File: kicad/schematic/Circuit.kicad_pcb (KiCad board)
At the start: 2 copper layers, 66 parts, among them P1 LED+, P10 1MTR+, P11 1MTR+, P12 1MTR+, P13 1MTR+, P14 1MTR+, P15 1MTR+, P16 1MTR+, P17 1MTR+, P18 1MTR+, P19 1MTR+, P2 LED+, P20 1MTR+, P22 1MTR+, P3 LED+, P4 PWR+, P5 PWR-, P6 1MTR+, P7 1MTR+, P8 1MTR+, P9 1MTR+, Q1 AO3400A, Q2 AO3400A, Q3 AO3400A, Q4 AO3400A, Q5 AO3400A, Q6 AO3400A, Q7 AO3400A, Q8 AO3400A

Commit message: changed board layout. WIP
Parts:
- removed P1, P2, P3: LED+, Connector_Wire:SolderWirePad_1x01_SMD_1x2mm
- removed P10, P11, P12, P13, P14, P15, P16, P17, P18, P19, P20, P22, P6, P7, P8, P9: 1MTR+, Connector_Wire:SolderWirePad_1x01_SMD_1x2mm
- removed P4: PWR+, Connector_Wire:SolderWirePad_1x01_SMD_1x2mm
- removed P5: PWR-, Connector_Wire:SolderWirePad_1x01_SMD_1x2mm
- added BAT+1: ~, ESP_global:blank pad, F.Cu at (162.6, 87.0)
- added BAT-1: ~, ESP_global:blank pad, F.Cu at (162.6, 89.5)
- added C9: C_Polarized, Capacitor_SMD:CP_Elec_8x10.5, F.Cu at (209.6, 94.5)
- added R19: R, Resistor_SMD:R_0805_2012Metric, F.Cu at (205.1, 102.5)
- added RGB-DIN1: ~, ESP_global:blank pad, F.Cu at (205.1, 107.3)
- added RGB-VDD1: ~, ESP_global:blank pad, F.Cu at (207.6, 107.3)
- added RGB-gnd1: ~, ESP_global:blank pad, F.Cu at (210.2, 107.3)
- added m1+1: ~, ESP_global:blank pad, F.Cu at (227.3, 64.1)
- added m1-1: ~, ESP_global:blank pad, F.Cu at (227.3, 61.6)
- added m2+1: ~, ESP_global:blank pad, F.Cu at (227.3, 70.5)
- added m2-1: ~, ESP_global:blank pad, F.Cu at (227.3, 67.9)
- added m3+1: ~, ESP_global:blank pad, F.Cu at (227.3, 76.8)
- added m3-1: ~, ESP_global:blank pad, F.Cu at (227.3, 74.3)
- added m4+1: ~, ESP_global:blank pad, F.Cu at (227.3, 83.2)
- added m4-1: ~, ESP_global:blank pad, F.Cu at (227.3, 80.6)
- added m5+1: ~, ESP_global:blank pad, F.Cu at (227.3, 89.5)
- added m5-1: ~, ESP_global:blank pad, F.Cu at (227.3, 87.0)
- added m6+1: ~, ESP_global:blank pad, F.Cu at (215.9, 107.3)
- added m6-1: ~, ESP_global:blank pad, F.Cu at (213.4, 107.3)
- added m7+1: ~, ESP_global:blank pad, F.Cu at (219.7, 107.3)
- added m7-1: ~, ESP_global:blank pad, F.Cu at (222.2, 107.3)
- added m8+1: ~, ESP_global:blank pad, F.Cu at (226.1, 107.3)
- added m8-1: ~, ESP_global:blank pad, F.Cu at (228.6, 107.3)
- R17: value R 20k -> R
- R18: value R 10k -> R
- moved U2 111.1 mm to (198.1, 97.2), turned to 90 degrees
- moved Q8 105.7 mm to (197.2, 62.9)
- moved C8 105.4 mm to (228.0, 95.2), turned to -90 degrees
- moved R17 98.6 mm to (178.2, 89.5)
- moved D8 97.9 mm to (227.3, 100.9)
- moved R18 97.0 mm to (183.2, 89.5)
- moved C7 96.5 mm to (223.5, 95.2), turned to -90 degrees
- moved D7 89.1 mm to (222.9, 100.9)
- moved C6 88.7 mm to (218.4, 94.9), turned to -90 degrees
- moved Q7 86.5 mm to (197.2, 79.4)
- moved Q4 86.5 mm to (209.9, 83.2)
- moved Q6 85.5 mm to (197.2, 71.1)
- moved R8 85.3 mm to (205.4, 76.2), turned to 0 degrees
- moved R3 85.0 mm to (205.5, 73.7), turned to 0 degrees
- moved Q3 84.9 mm to (209.9, 78.1)
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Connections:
- ESP32_S3_ZERO1 pad 8: unconnected-(ESP32_S3_ZERO1-GP5-Pad8) -> Net-(ESP32_S3_ZERO1-GP5)
- R10 pad 1: Net-(Q4-G) -> Net-(ESP32_S3_ZERO1-GP9)
- R12 pad 1: Net-(Q6-G) -> Net-(ESP32_S3_ZERO1-GP8)
- R14 pad 1: Net-(Q7-G) -> Net-(ESP32_S3_ZERO1-GP7)
- R16 pad 1: Net-(Q8-G) -> Net-(ESP32_S3_ZERO1-GP6)
- R6 pad 1: Net-(Q5-G) -> Net-(ESP32_S3_ZERO1-GP13)
- R7 pad 1: Net-(Q1-G) -> Net-(ESP32_S3_ZERO1-GP12)
- R8 pad 1: Net-(Q2-G) -> Net-(ESP32_S3_ZERO1-GP11)
- R9 pad 1: Net-(Q3-G) -> Net-(ESP32_S3_ZERO1-GP10)
- U1 pad 5: Net-(D1-K) -> Net-(U1-OUT+)
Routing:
- net GND: track 259.1 -> 0.00 mm, vias 21 -> 0
- net Net-(D1-K): track 257.6 -> 0.00 mm, vias 12 -> 0
- net GND1: track 82.8 -> 0.00 mm, vias 2 -> 0
- net Net-(ESP32_S3_ZERO1-GP7): track 67.4 -> 0.00 mm, vias 4 -> 0
- net Net-(ESP32_S3_ZERO1-GP13): track 63.8 -> 0.00 mm, vias 4 -> 0
- net Net-(ESP32_S3_ZERO1-GP8): track 60.9 -> 0.00 mm, vias 4 -> 0
- net Net-(ESP32_S3_ZERO1-GP9): track 53.7 -> 0.00 mm, vias 4 -> 0
- net Net-(ESP32_S3_ZERO1-GP6): track 53.5 -> 0.00 mm, vias 2 -> 0
- net Net-(ESP32_S3_ZERO1-GP12): track 49.8 -> 0.00 mm, vias 4 -> 0
- net Net-(ESP32_S3_ZERO1-GP10): track 47.2 -> 0.00 mm, vias 4 -> 0
- net Net-(ESP32_S3_ZERO1-GP11): track 39.2 -> 0.00 mm, vias 2 -> 0
- net Net-(ESP32_S3_ZERO1-5V): track 34.5 -> 0.00 mm, vias 4 -> 0
- net Net-(ESP32_S3_ZERO1-GP1): track 16.4 -> 0.00 mm, vias 2 -> 0
- net Net-(D6-A): track 12.4 -> 0.00 mm
- net Net-(D8-A): track 12.3 -> 0.00 mm
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
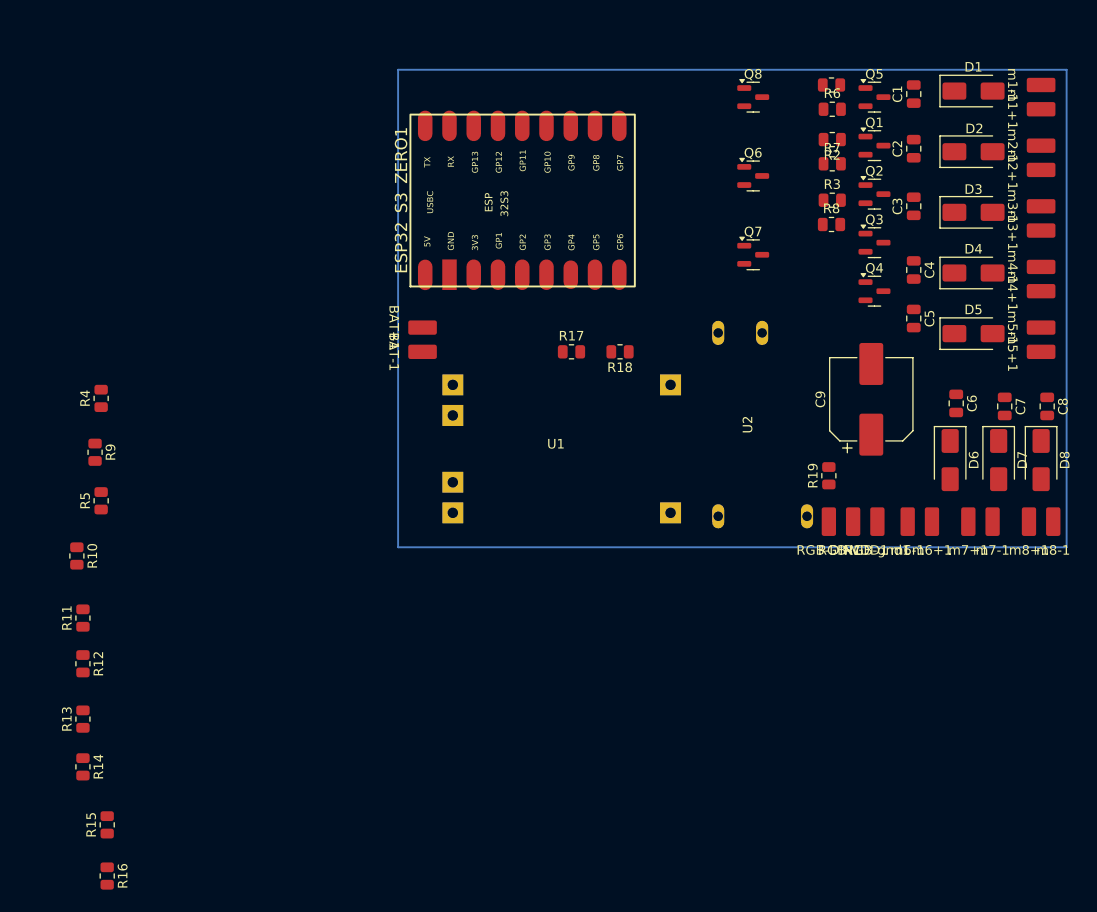
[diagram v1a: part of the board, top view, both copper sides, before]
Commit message: Alle Komponenten auf dem Board - Leiterbahnen verlegt
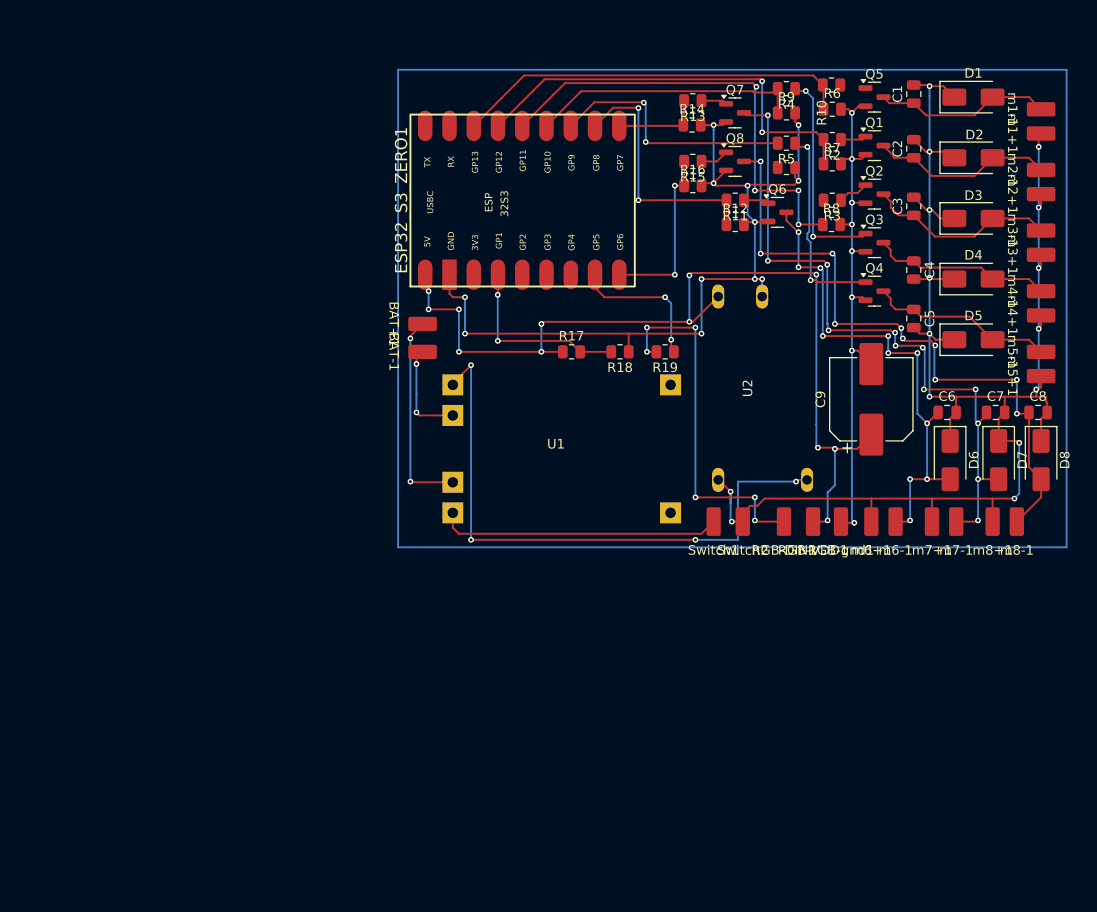
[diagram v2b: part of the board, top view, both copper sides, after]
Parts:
- added Switch1: ~, ESP_global:blank pad, F.Cu at (193.0, 107.3)
- added Switch2: ~, ESP_global:blank pad, F.Cu at (196.1, 107.3)
- moved R16 94.8 mm to (190.9, 72.1), turned to 0 degrees
- moved R15 92.7 mm to (190.9, 69.6), turned to 180 degrees
- moved R14 92.7 mm to (190.8, 65.8), turned to 0 degrees
- moved R13 90.9 mm to (190.9, 63.2), turned to 180 degrees
- moved R10 84.7 mm to (200.7, 70.2), turned to 0 degrees
- moved R12 82.3 mm to (195.3, 76.2), turned to 0 degrees
- moved R11 81.1 mm to (195.3, 73.7), turned to 180 degrees
- moved R5 80.9 mm to (200.7, 67.7), turned to 180 degrees
- moved R9 80.6 mm to (200.7, 64.5), turned to 0 degrees
- moved R4 78.7 mm to (200.7, 62.0), turned to 180 degrees
- moved R19 21.5 mm to (188.0, 89.5), turned to 180 degrees
- moved Q7 15.0 mm to (195.3, 64.5)
- moved Q8 7.00 mm to (195.3, 69.6)
- moved m6+1 6.35 mm to (209.6, 107.3)
- moved RGB-DIN1 4.70 mm to (200.4, 107.3)
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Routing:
- net Net-(D1-K): track 0.00 -> 170.4 mm, vias 0 -> 15
- net GND: track 0.00 -> 150.1 mm, vias 0 -> 20
- net Net-(ESP32_S3_ZERO1-5V): track 0.00 -> 97.0 mm, vias 0 -> 12
- net Net-(D7-A): track 0.00 -> 72.4 mm, vias 0 -> 12
- net Net-(D8-A): track 0.00 -> 68.5 mm, vias 0 -> 10
- net GND1: track 0.00 -> 62.5 mm, vias 0 -> 4
- net Net-(D6-A): track 0.00 -> 53.4 mm, vias 0 -> 11
- net Net-(ESP32_S3_ZERO1-GP11): track 0.00 -> 48.1 mm, vias 0 -> 4
- net Net-(ESP32_S3_ZERO1-GP12): track 0.00 -> 44.4 mm, vias 0 -> 2
- net Net-(ESP32_S3_ZERO1-GP13): track 0.00 -> 41.7 mm
- net Net-(RGB-DIN1-pin): track 0.00 -> 38.1 mm, vias 0 -> 6
- net Net-(Switch1-pin): track 0.00 -> 29.7 mm
- net Net-(ESP32_S3_ZERO1-GP10): track 0.00 -> 28.5 mm
- net Net-(ESP32_S3_ZERO1-GP9): track 0.00 -> 26.8 mm, vias 0 -> 2
- net Net-(ESP32_S3_ZERO1-GP8): track 0.00 -> 26.8 mm, vias 0 -> 2
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
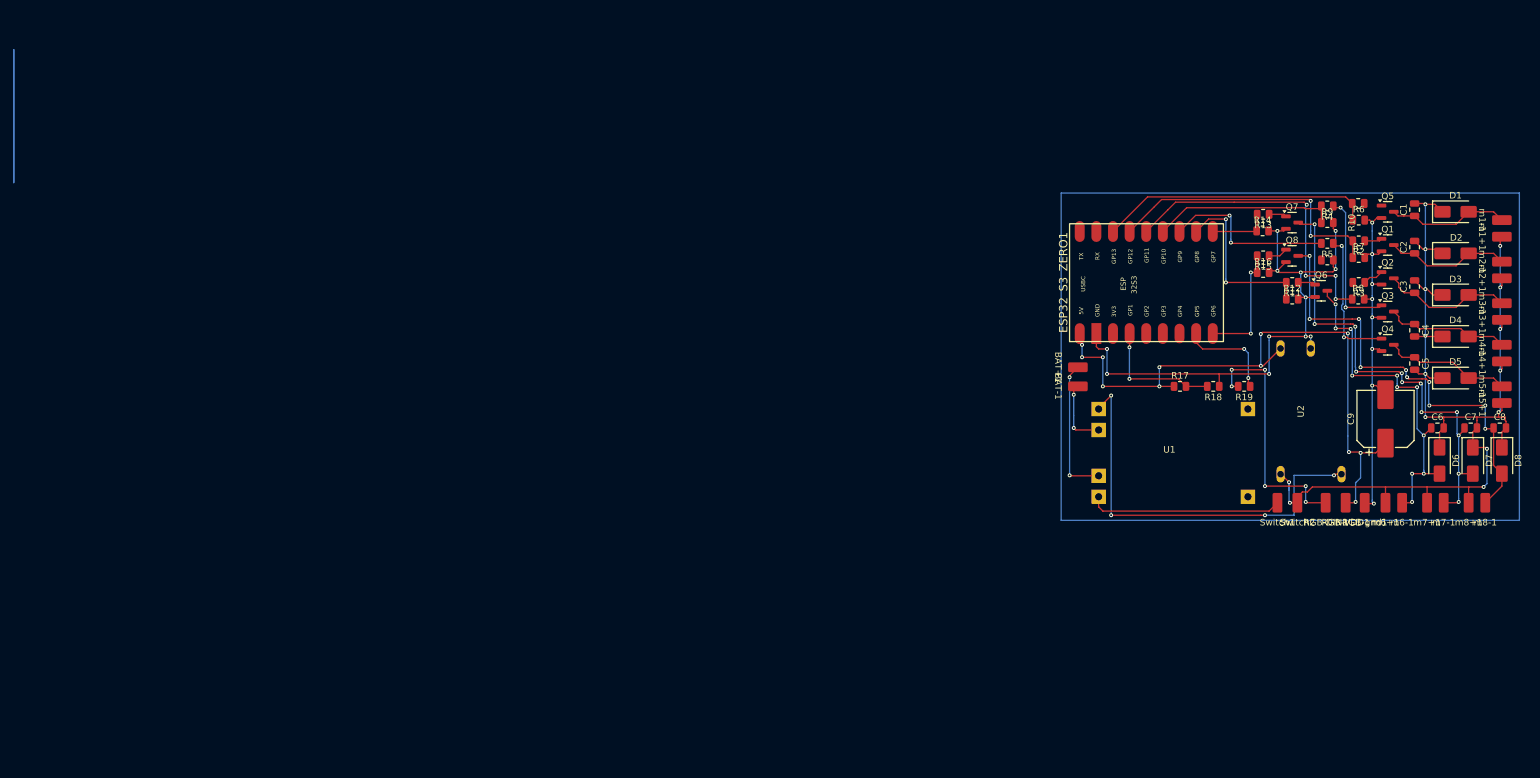
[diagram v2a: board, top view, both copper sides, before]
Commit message: fixed board size beschriftungen verbessert
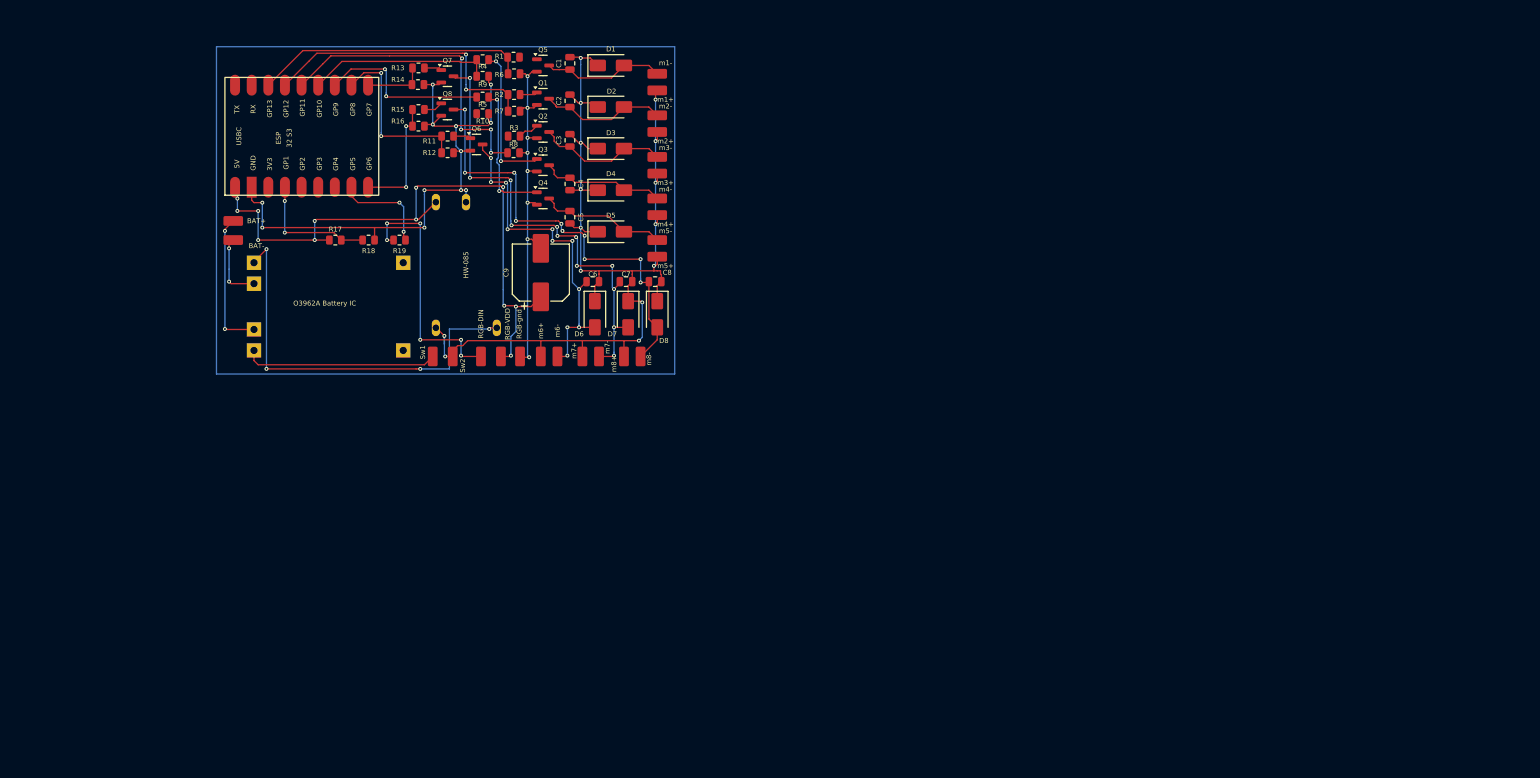
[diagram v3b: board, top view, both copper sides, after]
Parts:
- O3962A Battery IC: renamed from U1
- moved BAT+ 131.0 mm to (33.5, 64.3)
- moved BAT- 131.0 mm to (33.5, 67.2)
- moved C1 131.0 mm to (85.0, 40.2)
- moved C2 131.0 mm to (85.0, 45.9)
- moved C3 131.0 mm to (85.0, 51.9)
- moved C4 131.0 mm to (85.0, 58.6)
- moved C5 131.0 mm to (85.0, 63.7)
- moved C6 131.0 mm to (88.5, 73.5)
- moved C9 131.0 mm to (80.5, 72.2)
- moved D6 131.0 mm to (88.8, 78.5)
- moved D8 131.0 mm to (98.3, 78.5)
- moved HW-085 131.0 mm to (69.1, 71.0)
- moved O3962A Battery IC 131.0 mm to (47.5, 77.3)
- moved R11 131.0 mm to (66.3, 51.3)
- moved R12 131.0 mm to (66.3, 53.8)
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- renumbered BAT+1 to BAT+, BAT-1 to BAT-, U2 to HW-085, RGB-DIN1 to RGB-DIN, RGB-VDD1 to RGB-VDD, RGB-gnd1 to RGB-gnd, Switch1 to Sw1, Switch2 to Sw2, m1+1 to m1+, m1-1 to m1-, m2+1 to m2+, m2-1 to m2-, m3+1 to m3+, m3-1 to m3-, m4+1 to m4+, m4-1 to m4-, m5+1 to m5+, m5-1 to m5-, m6+1 to m6+, m6-1 to m6-, m7+1 to m7+, m7-1 to m7-, m8+1 to m8+, m8-1 to m8-
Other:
- board text added: "R1"
- board text added: "R13"
- board text added: "R14"

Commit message: turned Charging moved esp
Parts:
- moved O3962A Battery IC 2.29 mm to (45.2, 77.3), turned to 180 degrees
- moved ESP32_S3_ZERO1 2.01 mm to (46.0, 51.3)
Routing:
- net GND1: track 62.5 -> 25.1 mm, vias 4 -> 1
- net Net-(BAT-1-pin): track 10.5 -> 36.0 mm, vias 2 -> 1
- net Net-(BAT+1-pin): track 21.5 -> 31.4 mm, vias 2 -> 1
- net Net-(Switch1-pin): track 29.7 -> 20.5 mm, vias 0 -> 1
- net GND: track 150.1 -> 154.7 mm
- net Net-(Q5-G): track 0.00 -> 2.78 mm
- net Net-(ESP32_S3_ZERO1-GP1): track 19.3 -> 17.3 mm
- net Net-(ESP32_S3_ZERO1-GP6): track 18.7 -> 16.6 mm
- net Net-(ESP32_S3_ZERO1-GP7): track 9.32 -> 7.31 mm
- net Net-(ESP32_S3_ZERO1-5V): track 97.0 -> 95.2 mm, vias 12 -> 10
- net Net-(ESP32_S3_ZERO1-GP5): track 15.2 -> 13.8 mm
- net Net-(ESP32_S3_ZERO1-GP12): track 44.4 -> 43.6 mm
- net Net-(ESP32_S3_ZERO1-GP10): track 28.5 -> 27.6 mm
- net Net-(ESP32_S3_ZERO1-GP13): track 41.7 -> 40.9 mm
- net Net-(ESP32_S3_ZERO1-GP11): track 48.1 -> 47.3 mm
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
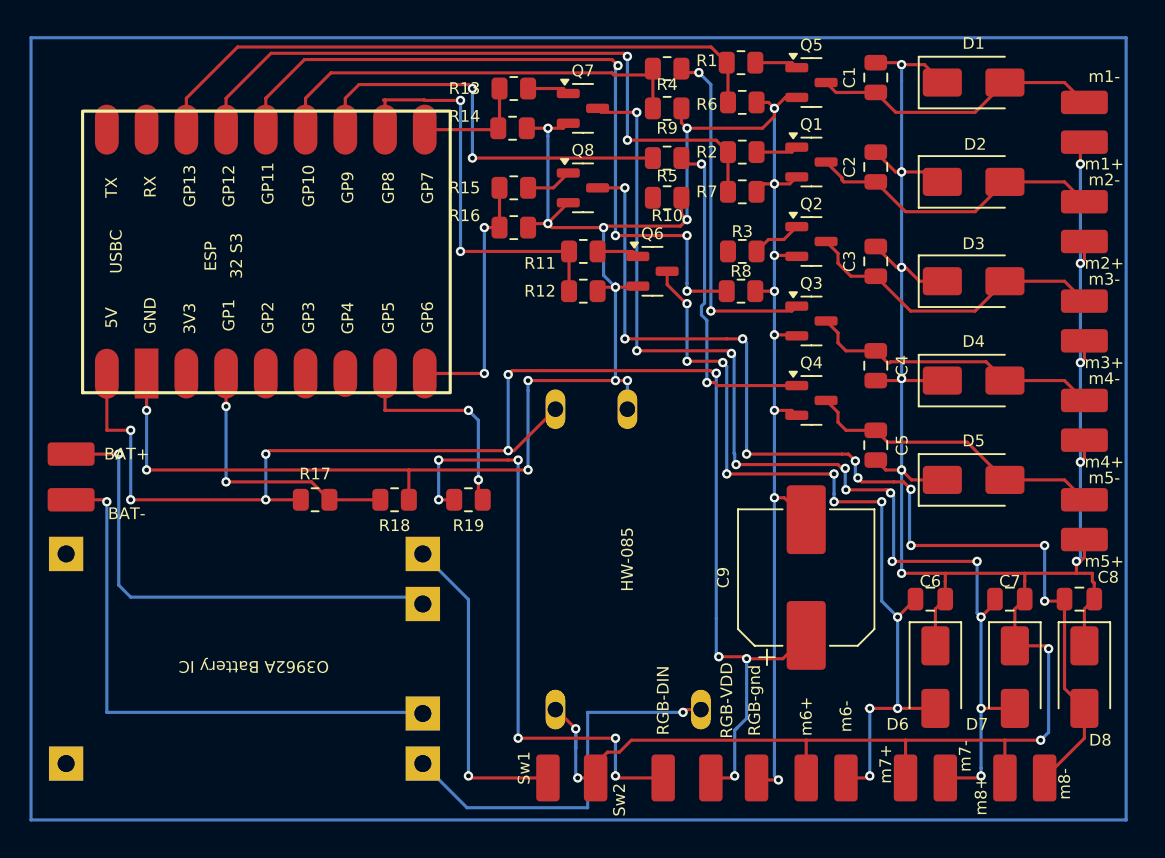
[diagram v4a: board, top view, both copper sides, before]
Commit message: changed pads HW-085
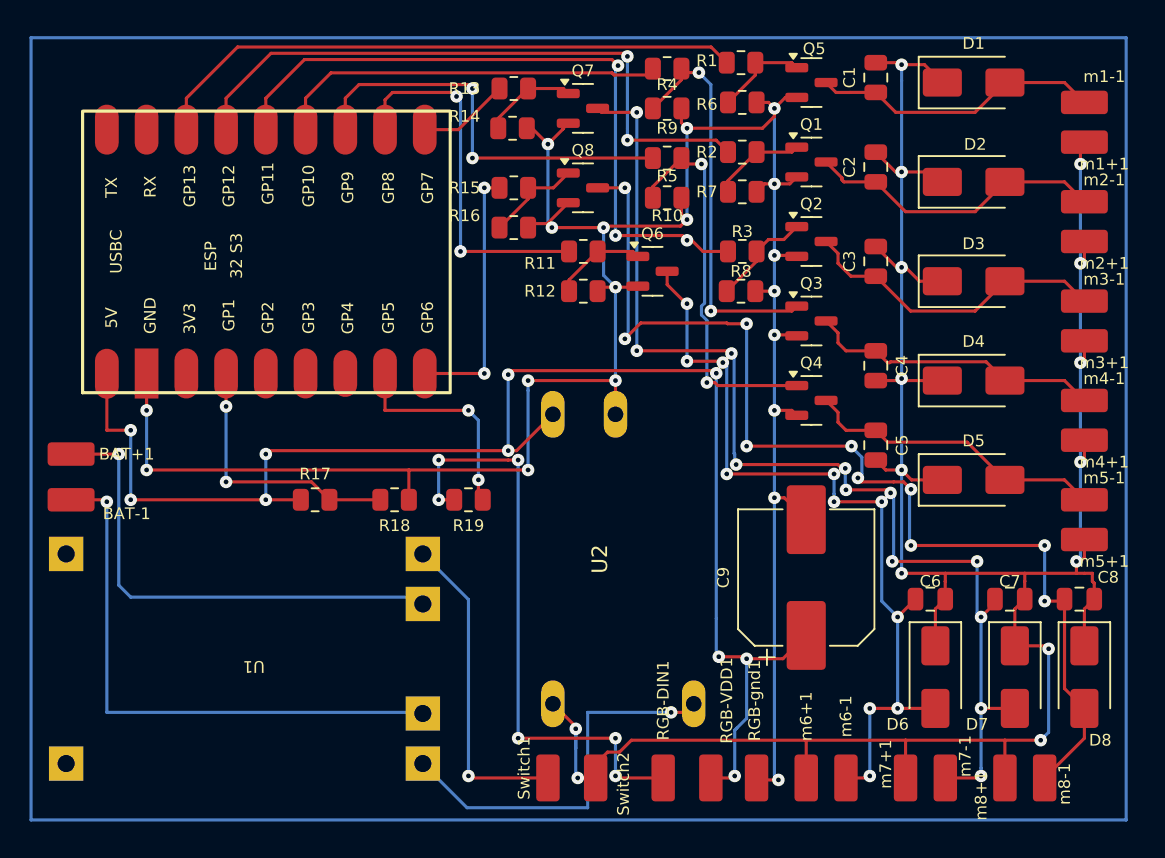
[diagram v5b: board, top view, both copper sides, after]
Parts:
- removed HW-085: ~, ESP_global:HW-085
- added U2: ~, ESP_global:HW-085, F.Cu at (68.8, 71.0)
- U1: renamed from O3962A Battery IC
- renumbered BAT+ to BAT+1, BAT- to BAT-1, RGB-DIN to RGB-DIN1, RGB-VDD to RGB-VDD1, RGB-gnd to RGB-gnd1, Sw1 to Switch1, Sw2 to Switch2, m1+ to m1+1, m1- to m1-1, m2+ to m2+1, m2- to m2-1, m3+ to m3+1, m3- to m3-1, m4+ to m4+1, m4- to m4-1, m5+ to m5+1, m5- to m5-1, m6+ to m6+1, m6- to m6-1, m7+ to m7+1, m7- to m7-1, m8+ to m8+1, m8- to m8-1
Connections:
- R10 pad 1: Net-(ESP32_S3_ZERO1-GP9) -> Net-(Q4-G)
- R12 pad 1: Net-(ESP32_S3_ZERO1-GP8) -> Net-(Q6-G)
- R14 pad 1: Net-(ESP32_S3_ZERO1-GP7) -> Net-(Q7-G)
- R16 pad 1: Net-(ESP32_S3_ZERO1-GP6) -> Net-(Q8-G)
- R6 pad 1: Net-(ESP32_S3_ZERO1-GP13) -> Net-(Q5-G)
- R7 pad 1: Net-(ESP32_S3_ZERO1-GP12) -> Net-(Q1-G)
- R8 pad 1: Net-(ESP32_S3_ZERO1-GP11) -> Net-(Q2-G)
- R9 pad 1: Net-(ESP32_S3_ZERO1-GP10) -> Net-(Q3-G)
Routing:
- net Net-(Q2-G): track 3.23 -> 6.56 mm
- net Net-(Q7-G): track 2.70 -> 6.03 mm
- net Net-(Q8-G): track 2.96 -> 6.26 mm
- net Net-(Q1-G): track 2.70 -> 6.00 mm
- net Net-(Q6-G): track 2.70 -> 6.00 mm
- net Net-(Q4-G): track 21.5 -> 24.8 mm
- net Net-(Q3-G): track 22.4 -> 25.7 mm
- net Net-(Q5-G): track 2.78 -> 6.05 mm
- net Net-(ESP32_S3_ZERO1-GP11): track 47.3 -> 44.2 mm, vias 4 -> 3
- net Net-(ESP32_S3_ZERO1-GP13): track 40.9 -> 38.3 mm
- net Net-(ESP32_S3_ZERO1-GP12): track 43.6 -> 41.0 mm
- net Net-(ESP32_S3_ZERO1-GP10): track 27.6 -> 25.1 mm
- net Net-(ESP32_S3_ZERO1-GP8): track 26.0 -> 23.7 mm
- net Net-(D8-A): track 68.5 -> 70.6 mm
- net Net-(ESP32_S3_ZERO1-GP7): track 7.31 -> 5.87 mm
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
